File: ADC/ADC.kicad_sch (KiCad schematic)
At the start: 1 part

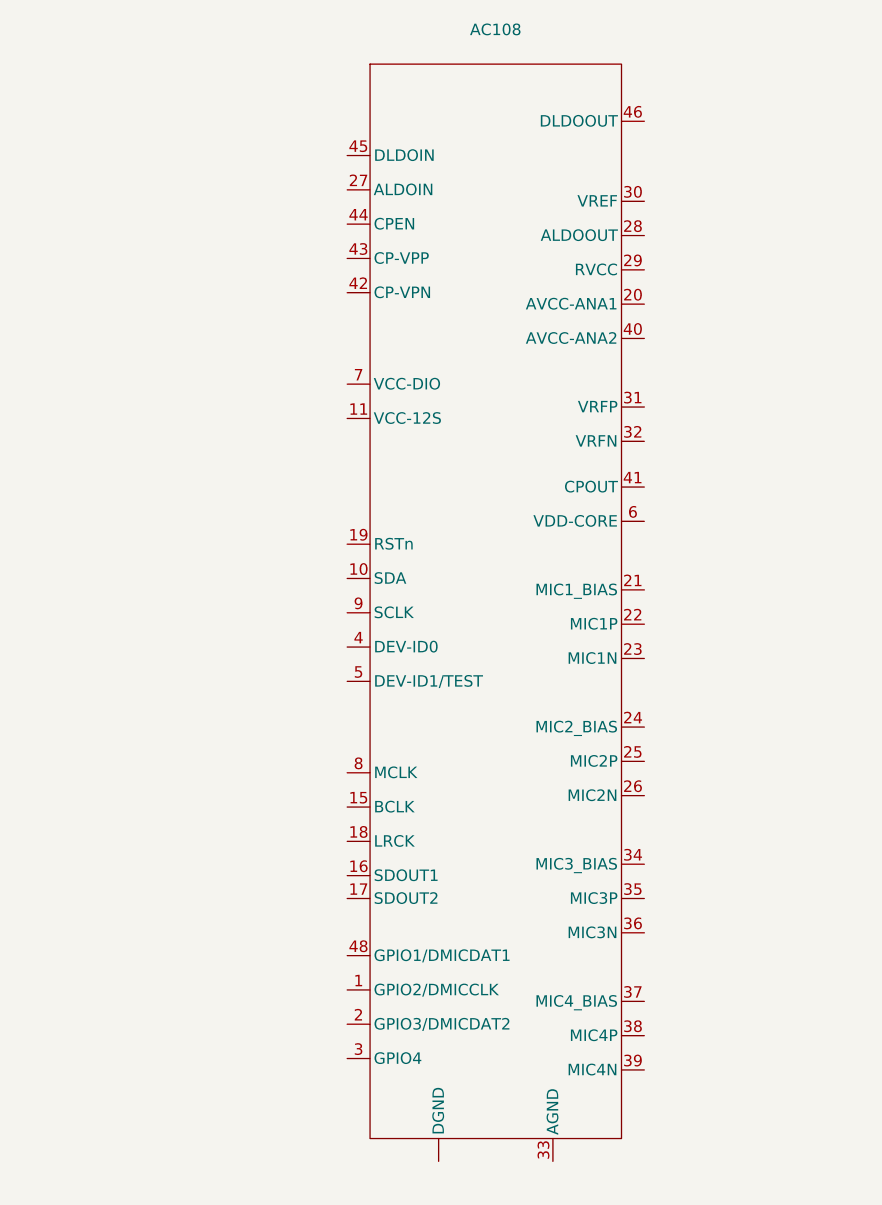
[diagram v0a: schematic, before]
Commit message: Updated KiCAD library to CCB standard.  Added reverse engineering document files.
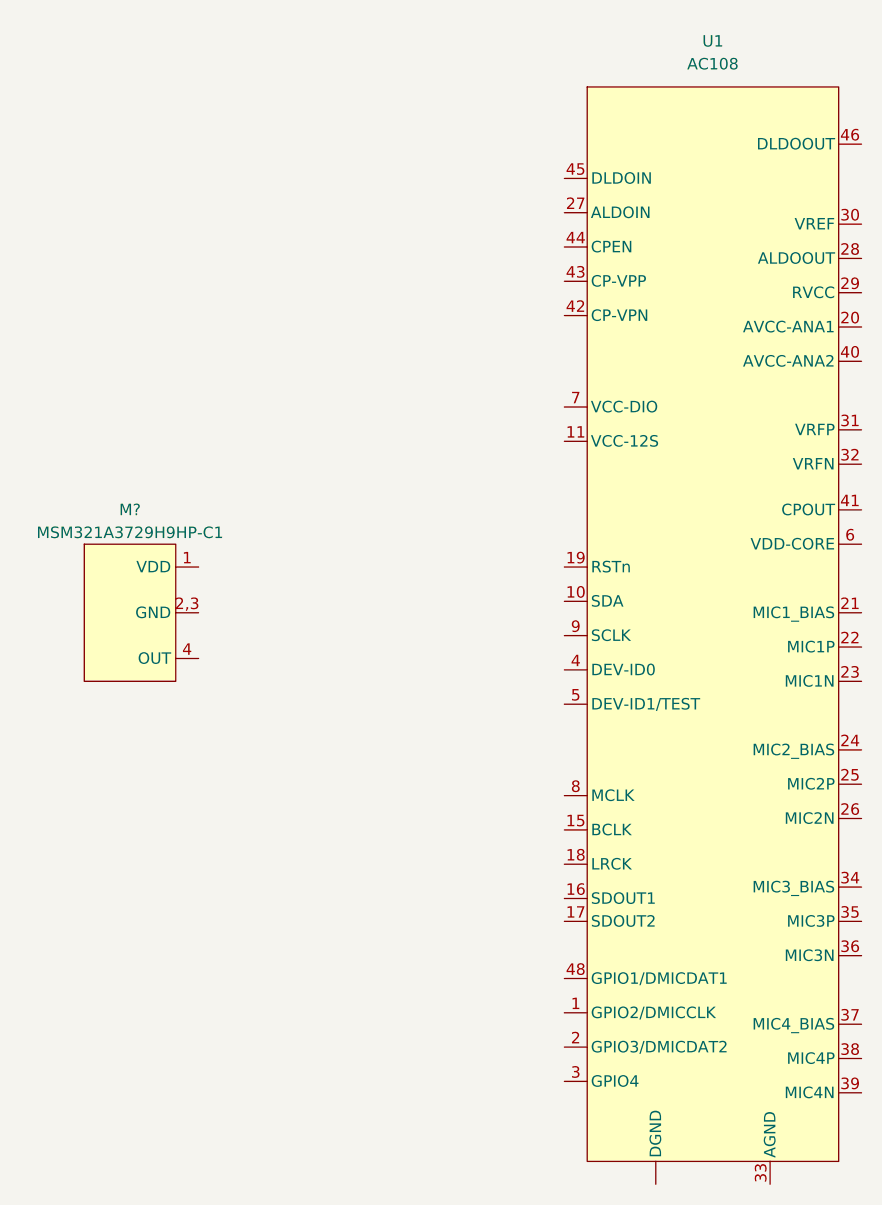
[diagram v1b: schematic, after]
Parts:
- removed AC108: ~, Library:AC108, symbol AC108:AC108
- added M?: MSM321A3729H9HP-C1, ccb_microphone:MSM321A3729H8HP-C_FP, symbol ccb_microphone:MSM321A3729H9HP-C
- added U1: AC108, ccb_package_DFN_QFN:AC108, symbol ccb_ADC:AC108
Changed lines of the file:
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@@
 	(paper "A4")
 	(symbol
-		(lib_id "AC108:AC108")
-		(at 116.84 87.63 0)
+		(lib_id "ccb_microphone:MSM321A3729H9HP-C")
+		(at 76.2 92.71 0)
 		(unit 1)
 		(exclude_from_sim no)
@@
 		(dnp no)
 		(fields_autoplaced yes)
-		(property "Reference" "AC108"
-			(at 116.84 27.94 0)
-			(effects
-				(font
-					(size 1.27 1.27)
-				)
-			)
-		)
-		(property "Value" "~"
-			(at 116.84 30.48 0)
-			(effects
-				(font
-					(size 1.27 1.27)
-				)
-			)
-		)
-		(property "Footprint" "Library:AC108"
-			(at 116.84 26.67 0)
+		(property "Reference" "M?"
+			(at 76.2 81.28 0)
+			(effects
+				(font
+					(size 1.27 1.27)
+				)
+			)
+		)
+		(property "Value" "MSM321A3729H9HP-C1"
+			(at 76.2 83.82 0)
+			(effects
+				(font
+					(size 1.27 1.27)
+				)
+			)
+		)
+		(property "Footprint" "ccb_microphone:MSM321A3729H8HP-C_FP"
+			(at 76.2 92.71 0)
 			(effects
 				(font
@@
 		)
 		(property "Datasheet" ""
-			(at 116.84 26.67 0)
+			(at 76.2 92.71 0)
 			(effects
 				(font
@@
 		)
 		(property "Description" ""
-			(at 116.84 26.67 0)
-			(effects
-				(font
-					(size 1.27 1.27)
-				)
-				(hide yes)
-			)
-		)
-		(pin "19"
-		)
-		(pin "27"
-		)
-		(pin "23"
-		)
-		(pin "3"
-		)
-		(pin "15"
-		)
-		(pin "32"
-		)
-		(pin "35"
+			(at 76.2 92.71 0)
+			(effects
+				(font
+					(size 1.27 1.27)
+				)
+				(hide yes)
+			)
+		)
+		(pin "2,3"
 		)
 		(pin "1"
 		)
-		(pin "16"
-		)
-		(pin "21"
-		)
-		(pin "31"
-		)
-		(pin "36"
-		)
-		(pin "37"
-		)
-		(pin "38"
-		)
-		(pin "45"
-		)
-		(pin "48"
-		)
-		(pin "39"
-		)
-		(pin "5"
-		)
-		(pin "25"
-		)
-		(pin "18"
-		)
-		(pin "42"
-		)
-		(pin "17"
-		)
-		(pin "29"
-		)
-		(pin "46"
-		)
-		(pin "6"
-		)
-		(pin "34"
-		)
-		(pin "44"
-		)
-		(pin "7"
-		)
-		(pin "8"
-		)
-		(pin "9"
-		)
 		(pin "4"
-		)
-		(pin "33"
-		)
-		(pin "41"
-		)
-		(pin "22"
-		)
-		(pin "30"
-		)
-		(pin "40"
-		)
-		(pin "26"
-		)
-		(pin "43"
-		)
-		(pin "10"
-		)
-		(pin "2"
-		)
-		(pin "11"
-		)
-		(pin "20"
-		)
-		(pin "24"
-		)
-		(pin "28"
-		)
-		(pin ""
 		)
 		(instances
 			(project ""
 				(path "/7b6d95de-464f-4091-a404-a6fd0874107f"
-					(reference "AC108")
+					(reference "M?")
 					(unit 1)
 				)
+			)
+		)
+	)
+	(symbol
+		(lib_id "ccb_ADC:AC108")
+		(at 140.97 90.17 0)
+		(unit 1)
+		(exclude_from_sim no)
+		(in_bom yes)
+		(on_board yes)
+		(dnp no)
+		(fields_autoplaced yes)
+		(property "Reference" "U1"
+			(at 140.97 29.21 0)
+			(effects
+				(font
+					(size 1.27 1.27)
+				)
+			)
+		)
+		(property "Value" "AC108"
+			(at 140.97 31.75 0)
+			(effects
+				(font
+					(size 1.27 1.27)
+				)
+			)
+		)
+		(property "Footprint" "ccb_package_DFN_QFN:AC108"
+			(at 140.97 29.21 0)
+			(effects
+				(font
+					(size 1.27 1.27)
+				)
+				(hide yes)
+			)
+		)
+		(property "Datasheet" "https://cdn.sparkfun.com/assets/6/0/d/c/a/AC108_Datasheet_V1.1.pdf"
+			(at 140.97 29.21 0)
+			(effects
+				(font
+					(size 1.27 1.27)
+				)
+				(hide yes)
+			)
+		)
+		(property "Description" ""
+			(at 140.97 29.21 0)
+			(effects
+				(font
+					(size 1.27 1.27)
+				)
+				(hide yes)
+			)
+		)
+		(property "Manufacturer" ""
+			(at 140.97 90.17 0)
+			(effects
+				(font
+					(size 1.27 1.27)
+				)
+				(hide yes)
+			)
+		)
+		(property "MPN" ""
+			(at 140.97 90.17 0)
+			(effects
+				(font
+					(size 1.27 1.27)
+				)
+				(hide yes)
+			)
+		)
+		(property "Type" "SMD"
+			(at 140.97 90.17 0)
+			(effects
+				(font
+					(size 1.27 1.27)
+				)
+				(hide yes)
+			)
+		)
+		(pin "25"
+		)
+		(pin "29"
+		)
+		(pin "41"
+		)
+		(pin "2"
+		)
+		(pin "27"
+		)
+		(pin "15"
+		)
+		(pin "35"
+		)
+		(pin "10"
+		)
+		(pin "28"
+		)
+		(pin "26"
+		)
+		(pin "16"
+		)
+		(pin "32"
+		)
+		(pin "34"
+		)
+		(pin "11"
+		)
+		(pin "30"
+		)
+		(pin "37"
+		)
+		(pin "31"
+		)
+		(pin "8"
+		)
+		(pin "38"
+		)
+		(pin "39"
+		)
+		(pin "42"
+		)
+		(pin "43"
+		)
+		(pin "44"
+		)
+		(pin "40"
+		)
+		(pin "36"
+		)
+		(pin "45"
+		)
+		(pin "23"
+		)
+		(pin "33"
+		)
+		(pin "24"
+		)
+		(pin "46"
+		)
+		(pin "48"
+		)
+		(pin "17"
+		)
+		(pin ""
+		)
+		(pin "1"
+		)
+		(pin "4"
+		)
+		(pin "3"
+		)
+		(pin "20"
+		)
+		(pin "18"
+		)
+		(pin "19"
+		)
+		(pin "21"
+		)
+		(pin "22"
+		)
+		(pin "5"
+		)
+		(pin "7"
+		)
+		(pin "9"
+		)
+		(pin "6"
+		)
+		(instances
+			(project ""
+				(path "/7b6d95de-464f-4091-a404-a6fd0874107f"
+					(reference "U1")
+					(unit 1)
+				)

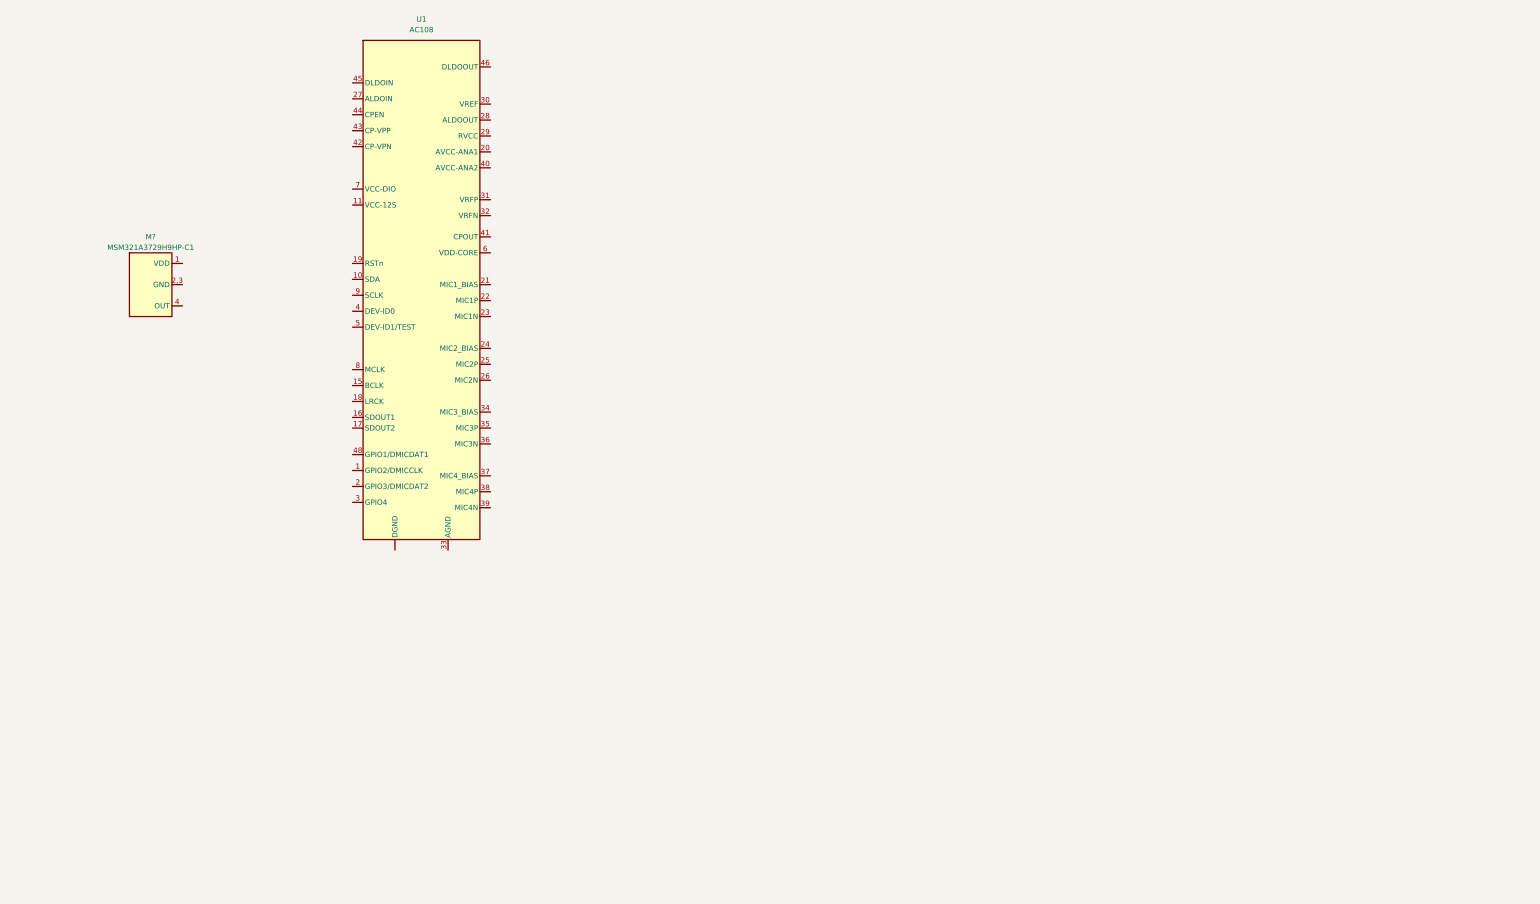
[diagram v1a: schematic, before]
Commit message: Initial schematic completed
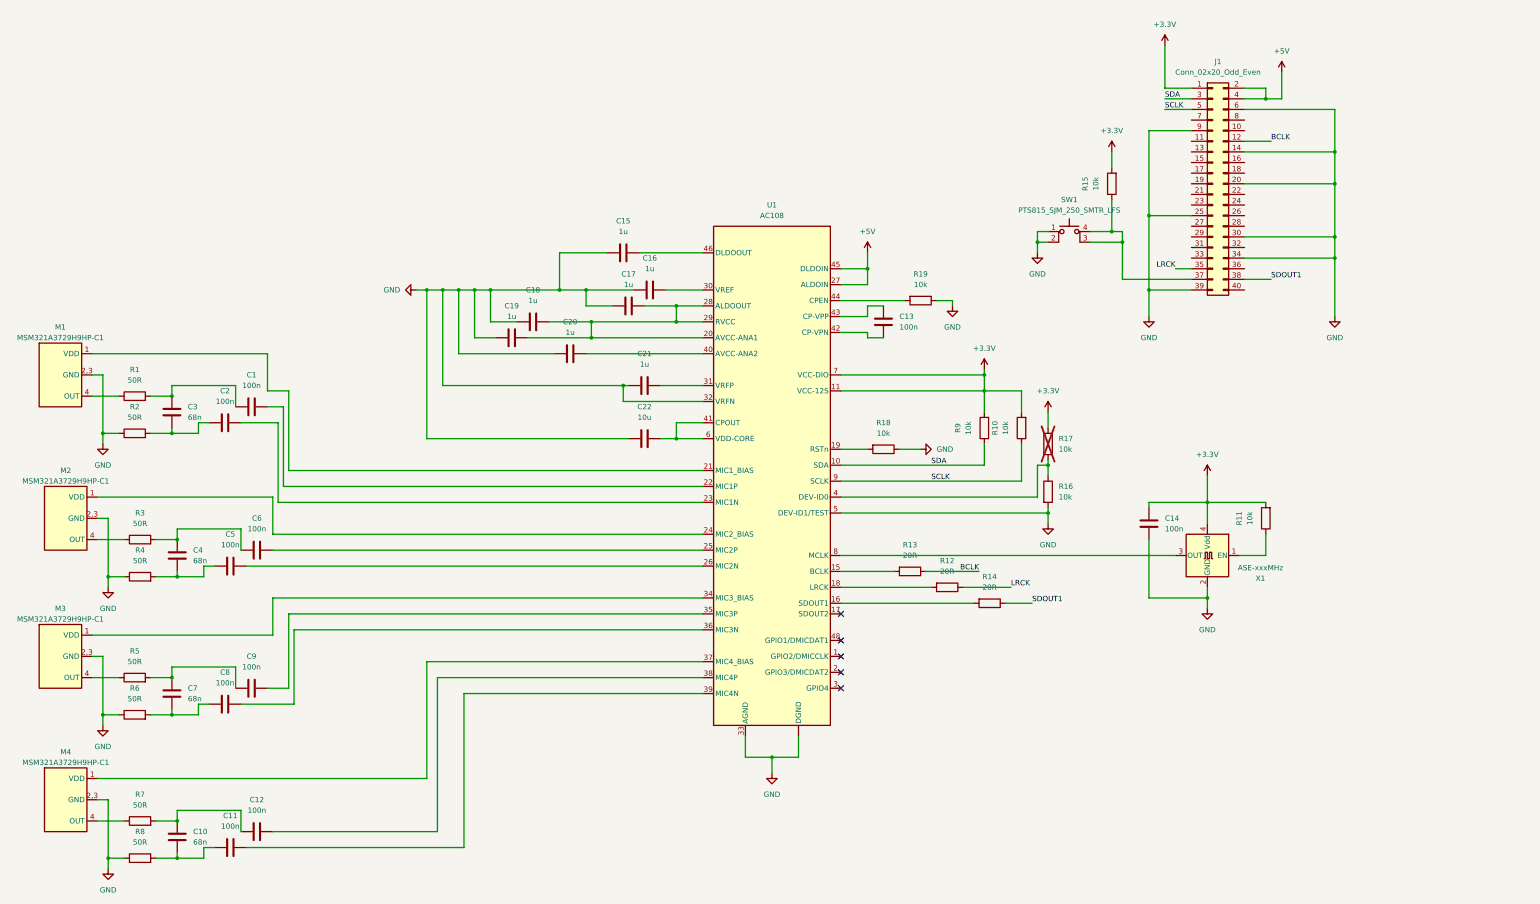
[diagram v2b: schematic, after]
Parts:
- removed M?: MSM321A3729H9HP-C1, ccb_microphone:MSM321A3729H8HP-C_FP, symbol ccb_microphone:MSM321A3729H9HP-C
- added C1, C11, C12, C13, C14, C2, C5, C6, C8, C9: 100n, symbol Device:C
- added C10, C3, C4, C7: 68n, symbol Device:C
- added C15, C16, C17, C18, C19, C20, C21: 1u, symbol Device:C
- added C22: 10u, symbol Device:C
- added J1: Conn_02x20_Odd_Even, Connector_PinSocket_2.54mm:PinSocket_2x20_P2.54mm_Vertical, symbol Connector_Generic:Conn_02x20_Odd_Even
- added M1, M2, M3, M4: MSM321A3729H9HP-C1, ccb_microphone:MSM321A3729H8HP-C_FP, symbol ccb_microphone:MSM321A3729H9HP-C
- added R1, R2, R3, R4, R5, R6, R7, R8: 50R, symbol Device:R
- added R10, R11, R15, R16, R17, R18, R19, R9: 10k, symbol Device:R
- added R12, R13, R14: 20R, symbol Device:R
- added SW1: PTS815_SJM_250_SMTR_LFS, ccb_button_switch:PTS815_SJM_250_SMTR_LFS, symbol ccb_button_switch:PTS815_SJM_250_SMTR_LFS
- added X1: ASE-xxxMHz, Oscillator:Oscillator_SMD_Abracon_ASE-4Pin_3.2x2.5mm, symbol Oscillator:ASE-xxxMHz
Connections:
- net GND: now reaches U1. (DGND)
- net GND: now also U1.32 (VRFN), U1.33 (AGND), U1.5 (DEV-ID1/TEST), C14.1, C15.1, C16.1, C17.1, C18.1, C19.1, C20.1, C21.1, C22.1, J1.14 (Pin_14), J1.20 (Pin_20), J1.25 (Pin_25), J1.30 (Pin_30), J1.34 (Pin_34), J1.39 (Pin_39), J1.6 (Pin_6), J1.9 (Pin_9), M1.2,3 (GND), M2.2,3 (GND), M3.2,3 (GND), M4.2,3 (GND), R16.2, R18.1, R19.1, R2.1, R4.1, R6.1, R8.1, SW1.1, SW1.2, X1.2 (GND)
- net SDA: now reaches U1.10 (SDA)
- net SDA: now also J1.3 (Pin_3), R9.1
- net +3.3V: now reaches U1.11 (VCC-12S)
- net +3.3V: now also U1.7 (VCC-DIO), C14.2, J1.1 (Pin_1), R10.2, R11.2, R15.2, R17.1, R9.2, X1.4 (Vdd)
- net at U1.15 (BCLK): now also R13.2
- net at U1.16 (SDOUT1): now also R14.2
- net at U1.18 (LRCK): now also R12.2
- net at U1.19 (RSTn): now also R18.2
- net at U1.20 (AVCC-ANA1): now also U1.28 (ALDOOUT), U1.29 (RVCC), C17.2, C18.2, C19.2
- net at U1.21 (MIC1_BIAS): now also M1.1 (VDD)
- net at U1.22 (MIC1P): now also C1.2
- net at U1.23 (MIC1N): now also C2.2
- net at U1.24 (MIC2_BIAS): now also M2.1 (VDD)
- net at U1.25 (MIC2P): now also C6.2
- net at U1.26 (MIC2N): now also C5.2
- net +5V: now reaches U1.27 (ALDOIN)
- net +5V: now also U1.45 (DLDOIN), J1.2 (Pin_2), J1.4 (Pin_4)
- net at U1.30 (VREF): now also C16.2
- net at U1.31 (VRFP): now also C21.2
- net at U1.34 (MIC3_BIAS): now also M3.1 (VDD)
- net at U1.35 (MIC3P): now also C9.2
- net at U1.36 (MIC3N): now also C8.2
- net at U1.37 (MIC4_BIAS): now also M4.1 (VDD)
- net at U1.38 (MIC4P): now also C12.2
- net at U1.39 (MIC4N): now also C11.2
- net at U1.4 (DEV-ID0): now also R16.1, R17.2
- net at U1.40 (AVCC-ANA2): now also C20.2
- net at U1.41 (CPOUT): now also U1.6 (VDD-CORE), C22.2
- net at U1.42 (CP-VPN): now also C13.1
- net at U1.43 (CP-VPP): now also C13.2
- net at U1.44 (CPEN): now also R19.2
- net at U1.46 (DLDOOUT): now also C15.2
- net at U1.8 (MCLK): now also X1.3 (OUT)
- net SCLK: now reaches U1.9 (SCLK)
- net SCLK: now also J1.5 (Pin_5), R10.1
- new net: M1.4 (OUT), R1.1
- new net: C1.1, C3.1, R1.2
- new net: C4.2, C5.1, R4.2
- new net: J1.37 (Pin_37), R15.1, SW1.3 (K), SW1.4 (A)
- new net: C4.1, C6.1, R3.2
- new net: M4.4 (OUT), R7.1
- new net: C2.1, C3.2, R2.2
- new net: C7.2, C8.1, R6.2
- new net: R11.1, X1.1 (EN)
- new net: C7.1, C9.1, R5.2
- new net: C10.1, C12.1, R7.2
- new net: M2.4 (OUT), R3.1
- new net: M3.4 (OUT), R5.1
- new net: C10.2, C11.1, R8.2
- new net BCLK: J1.12 (Pin_12), R13.1
- new net LRCK: J1.35 (Pin_35), R12.1
- new net SDOUT1: J1.38 (Pin_38), R14.1
- no-connect marks 0 -> 5
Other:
- company: (none) -> K.LISA YANG CCB
- title: (none) -> 4 CH MIC SCHEMATIC
- moved on the sheet: U1

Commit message: New layout for Mics
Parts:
- added D1: BLUE 0603, ccb_LED:LED_0603_1608Metric, symbol ccb_LED:EAST16084BA0
- added R20: 1k, ccb_resistor:R_0603_1608Metric, symbol Device:R
- added SW2: PTS815_SJM_250_SMTR_LFS, ccb_button_switch:PTS815_SJM_250_SMTR_LFS, symbol ccb_button_switch:PTS815_SJM_250_SMTR_LFS
- C1, C10, C11, C12, C13, C14, C15, C16, C17, C18, C19, C2, C20, C21, C22, C3, C4, C5, C6, C7, C8, C9: footprint (none) -> ccb_capacitor:C_0603_1608Metric
- R1, R10, R11, R12, R13, R14, R15, R16, R17, R18, R19, R2, R3, R4, R5, R6, R7, R8, R9: footprint (none) -> ccb_resistor:R_0603_1608Metric
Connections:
- net +5V: now also SW2.1, SW2.2
- net GND: now also R20.1
- new net: D1.2 (A), SW2.3 (K), SW2.4 (A)
- new net: D1.1 (K), R20.2
- no-connect marks 5 -> 28
